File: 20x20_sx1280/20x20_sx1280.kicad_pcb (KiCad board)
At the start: 2 copper layers, 25 x 25 mm, 20 parts, among them J1 Conn_01x04, SW1 SW_SPST, U1 ME6211C33, U2 ESP-01F, U3 LoRa1280

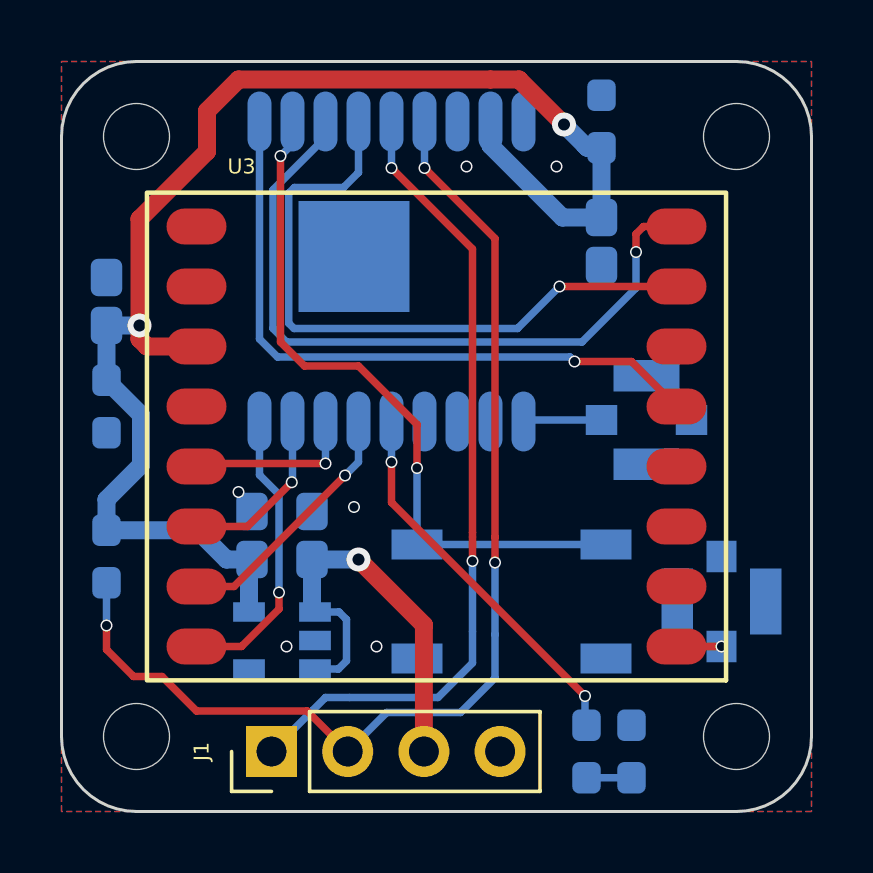
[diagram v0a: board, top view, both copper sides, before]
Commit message: Added minimal RX
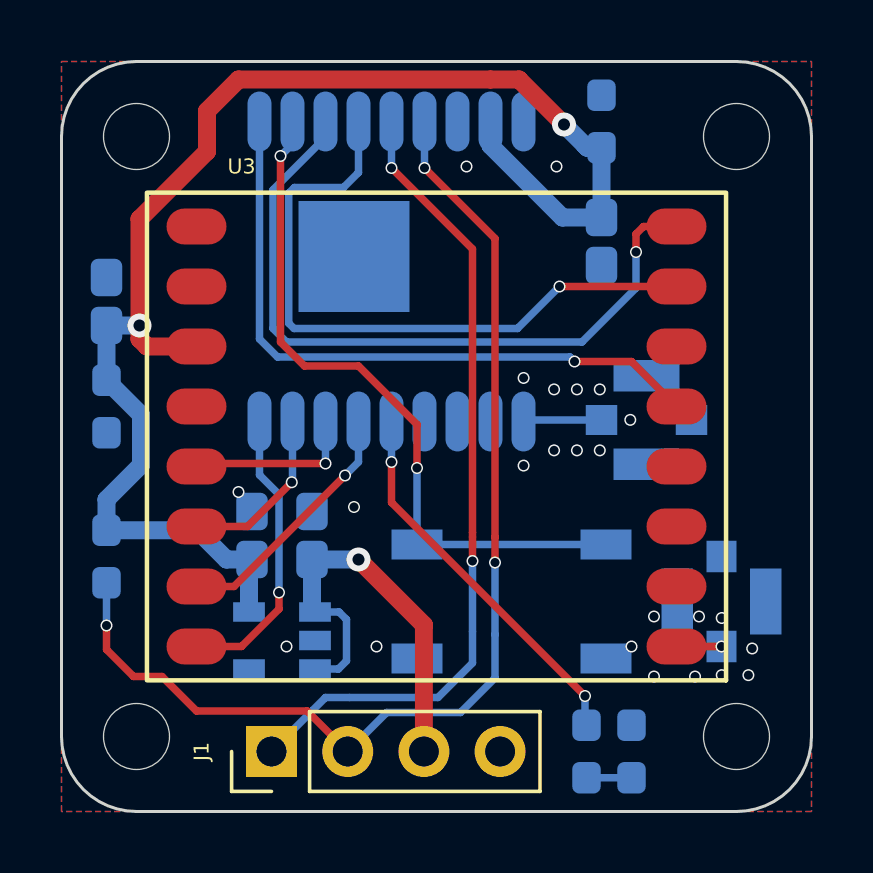
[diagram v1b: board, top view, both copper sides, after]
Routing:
- net GND: vias 6 -> 24
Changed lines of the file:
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@@
     (effects (font (size 0.5 0.5) (thickness 0.125)) (justify mirror))
   )
+  (via (at 117.25 146) (size 0.4) (drill 0.3) (layers "F.Cu" "B.Cu") (net 1))
+  (via (at 113.919 138.43) (size 0.4) (drill 0.3) (layers "F.Cu" "B.Cu") (net 1))
   (via (at 105 147) (size 0.4) (drill 0.3) (layers "F.Cu" "B.Cu") (net 1))
+  (via (at 112.903 140.97) (size 0.4) (drill 0.3) (layers "F.Cu" "B.Cu") (net 1))
+  (via (at 119.507 146.05) (size 0.4) (drill 0.3) (layers "F.Cu" "B.Cu") (net 1))
+  (via (at 114.681 138.43) (size 0.4) (drill 0.3) (layers "F.Cu" "B.Cu") (net 1))
+  (via (at 116.459 139.446) (size 0.4) (drill 0.3) (layers "F.Cu" "B.Cu") (net 1))
   (via (at 108 147) (size 0.4) (drill 0.3) (layers "F.Cu" "B.Cu") (net 1))
+  (via (at 112.903 138.049) (size 0.4) (drill 0.3) (layers "F.Cu" "B.Cu") (net 1))
+  (via (at 118.75 146) (size 0.4) (drill 0.3) (layers "F.Cu" "B.Cu") (net 1))
   (via (at 107.25 142.35) (size 0.4) (drill 0.3) (layers "F.Cu" "B.Cu") (net 1))
+  (via (at 117.25 148) (size 0.4) (drill 0.3) (layers "F.Cu" "B.Cu") (net 1))
   (via (at 114 131) (size 0.4) (drill 0.3) (layers "F.Cu" "B.Cu") (net 1))
+  (via (at 115.443 140.462) (size 0.4) (drill 0.3) (layers "F.Cu" "B.Cu") (net 1))
+  (via (at 113.919 140.462) (size 0.4) (drill 0.3) (layers "F.Cu" "B.Cu") (net 1))
+  (via (at 114.681 140.462) (size 0.4) (drill 0.3) (layers "F.Cu" "B.Cu") (net 1))
   (via (at 103.4 141.85) (size 0.4) (drill 0.3) (layers "F.Cu" "B.Cu") (net 1))
+  (via (at 118.618 148) (size 0.4) (drill 0.3) (layers "F.Cu" "B.Cu") (net 1))
+  (via (at 120.396 147.955) (size 0.4) (drill 0.3) (layers "F.Cu" "B.Cu") (net 1))
+  (via (at 119.507 147.955) (size 0.4) (drill 0.3) (layers "F.Cu" "B.Cu") (net 1))
   (via (at 111 131) (size 0.4) (drill 0.3) (layers "F.Cu" "B.Cu") (net 1))
+  (via (at 115.443 138.43) (size 0.4) (drill 0.3) (layers "F.Cu" "B.Cu") (net 1))
+  (via (at 116.5 147) (size 0.4) (drill 0.3) (layers "F.Cu" "B.Cu") (net 1))
+  (via (at 120.523 147.066) (size 0.4) (drill 0.3) (layers "F.Cu" "B.Cu") (net 1))
   (segment (start 115.5 139.45) (end 112.95 139.45) (width 0.25) (layer "B.Cu") (net 2))
   (segment (start 112.95 139.45) (end 112.9 139.5) (width 0.25) (layer "B.Cu") (net 2))
